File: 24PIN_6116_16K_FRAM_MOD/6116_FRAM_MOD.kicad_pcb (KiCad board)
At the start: 2 copper layers, 17.8 x 35.6 mm, 18 parts, among them J1 Conn_01x02, U1 TL431DBZ, U10 TC5564APL_Adapter, U2 74AHC2G00, U3 STK12C68

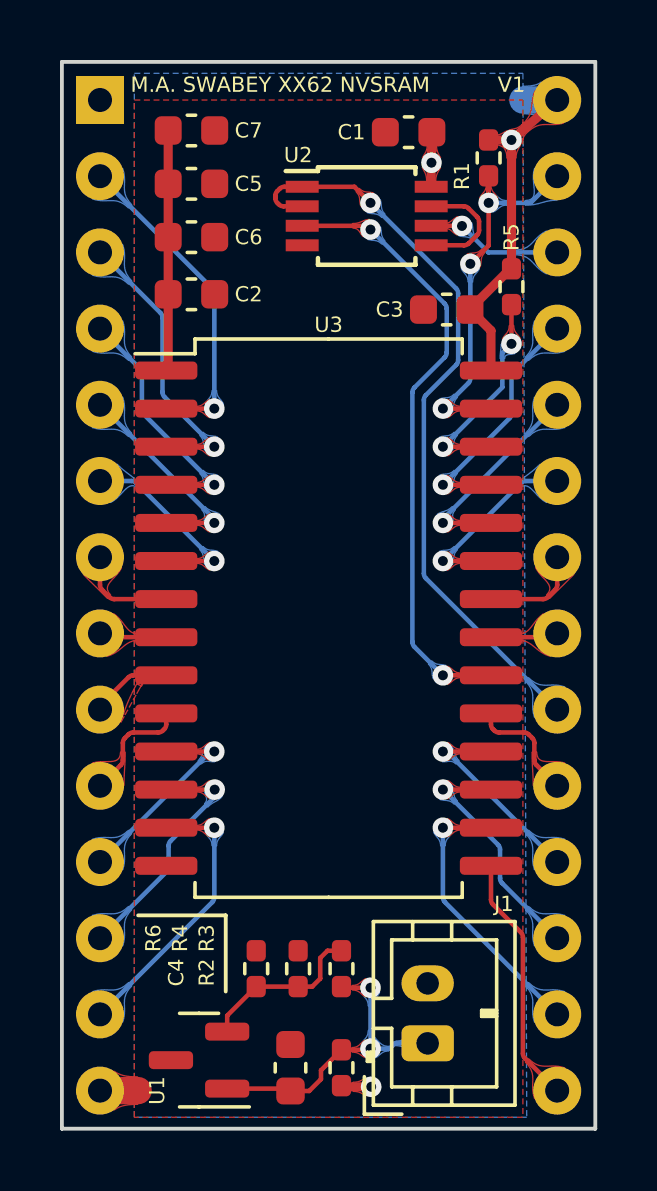
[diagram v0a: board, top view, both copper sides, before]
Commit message: Finished 24PIN 6116 version.
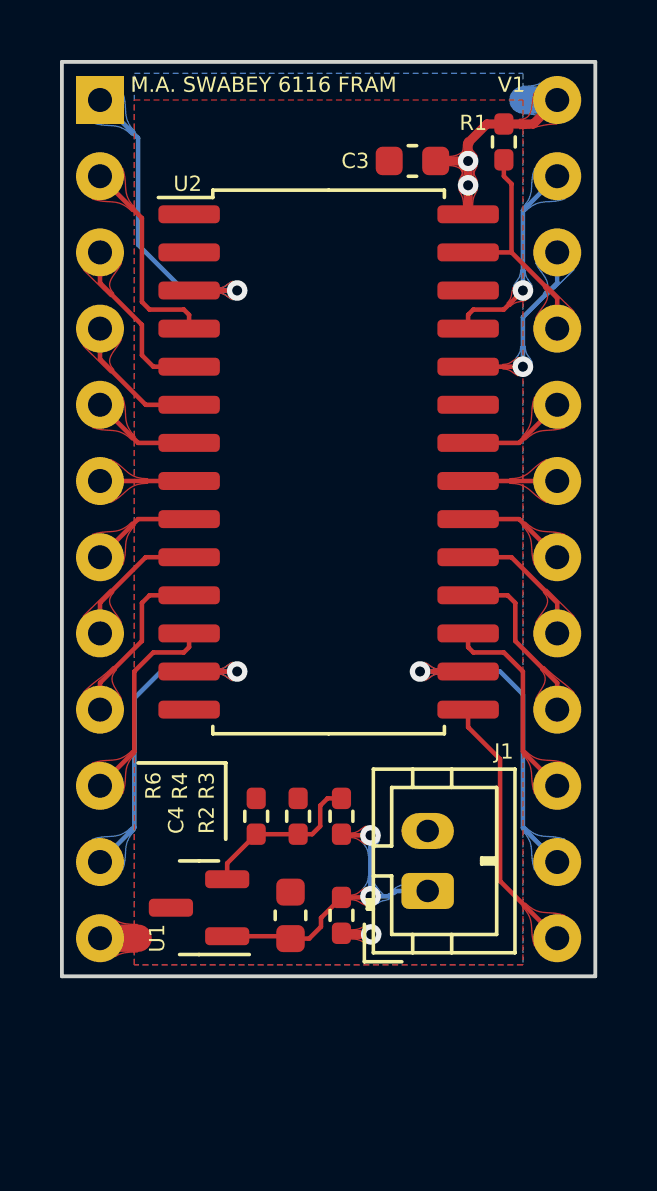
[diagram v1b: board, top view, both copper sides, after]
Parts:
- removed C1: 0.22u, Capacitor_SMD:C_0603_1608Metric
- removed C2, C5, C6, C7: 22u, Capacitor_SMD:C_0603_1608Metric
- removed R5: 10K, Resistor_SMD:R_0402_1005Metric_Pad0.72x0.64mm_HandSolder
- removed U3: STK12C68, Package_SO_Cypress:SOIC-28W_8.7x18.4mm_P1.27mm
- R1: value 10K -> 68K
- U10: footprint Package_DIP_Adapter:DIP-28_W15.24mm_Socket_Adapter -> Package_DIP_Adapter:DIP-24_W15.24mm_Socket_Adapter
- U2: value 74AHC2G00 -> FM16W08-SG; footprint Package_SO:TSSOP-8_3x3mm_P0.65mm -> Package_SO:SOIC-28W_7.5x17.9mm_P1.27mm
- moved U2 8.29 mm to (119.4, 70.5)
- moved C3 5.08 mm to (122.2, 60.5)
- moved U1 5.08 mm to (115.1, 85.3)
- moved C4 5.08 mm to (118.1, 85.6)
- moved J1 5.08 mm to (122.7, 84.8)
- moved R2 5.08 mm to (119.8, 85.6)
- moved R3 5.08 mm to (119.8, 82.3)
- moved R4 5.08 mm to (118.4, 82.3)
- moved R6 5.08 mm to (117.0, 82.3)
- moved R1 0.74 mm to (125.2, 59.8)
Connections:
- U10 pad 1: unconnected-(U10-Pad1) -> /A7
- U10 pad 10: /A0 -> /D1
- U10 pad 11: /D0 -> /D2
- U10 pad 12: /D1 -> GND
- U10 pad 13: /D2 -> /D3
- U10 pad 14: GND -> /D4
- U10 pad 15: /D3 -> /D5
- U10 pad 16: /D4 -> /D6
- U10 pad 17: /D5 -> /D7
- U10 pad 18: /D6 -> /~{CE}
- U10 pad 19: /D7 -> /A10
- U10 pad 2: /A12 -> /A6
- U10 pad 20: /~{CE1} -> /~{OE}
- U10 pad 21: /A10 -> /~{WE}
- U10 pad 22: /~{OE} -> /A9
- U10 pad 23: /A11 -> /A8
- U10 pad 24: /A9 -> VCC
- U10 pad 3: /A7 -> /A5
- U10 pad 4: /A6 -> /A4
- U10 pad 5: /A5 -> /A3
- U10 pad 6: /A4 -> /A2
- U10 pad 7: /A3 -> /A1
- U10 pad 8: /A2 -> /A0
- U10 pad 9: /A1 -> /D0
- U2 pad 1: /~{CE1} -> (no net)
- U2 pad 2: /~{CE1} -> GND
- U2 pad 3: /~{CE_STK} -> /A7
- U2 pad 4: GND -> /A6
- U2 pad 5: Net-(U2-Pad5) -> /A5
- U2 pad 6: /CE2 -> /A4
- U2 pad 7: Net-(U2-Pad5) -> /A3
- U2 pad 8: VCC -> /A2
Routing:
- net /~{CE1}: track 25.0 -> 0.00 mm, vias 1 -> 0
- net /~{CE_STK}: track 20.7 -> 0.00 mm, vias 2 -> 0
- net /A12: track 10.9 -> 0.00 mm, vias 1 -> 0
- net /VCAP: track 8.03 -> 0.00 mm
- net Net-(R5-Pad2): track 7.29 -> 0.00 mm, vias 2 -> 0
- net /A11: track 6.51 -> 0.00 mm, vias 1 -> 0
- net VCC: track 15.3 -> 9.18 mm
- net /~{WE}: track 13.5 -> 7.81 mm, vias 3 -> 0
- net /CE2: track 4.56 -> 0.00 mm, vias 1 -> 0
- net Net-(U2-Pad5): track 3.96 -> 0.00 mm
- net /~{CE}: track 0.00 -> 3.50 mm
- net /D4: track 9.39 -> 11.4 mm
- net /D2: track 9.39 -> 11.3 mm
- net /A4: track 6.51 -> 4.62 mm, vias 1 -> 0
- net /A8: track 8.37 -> 6.91 mm
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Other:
- board size 17.8 x 35.6 mm -> 17.8 x 30.5 mm
- board text added: "M.A. SWABEY 6116 FRAM"
- board text removed: "M.A. SWABEY XX62 NVSRAM"

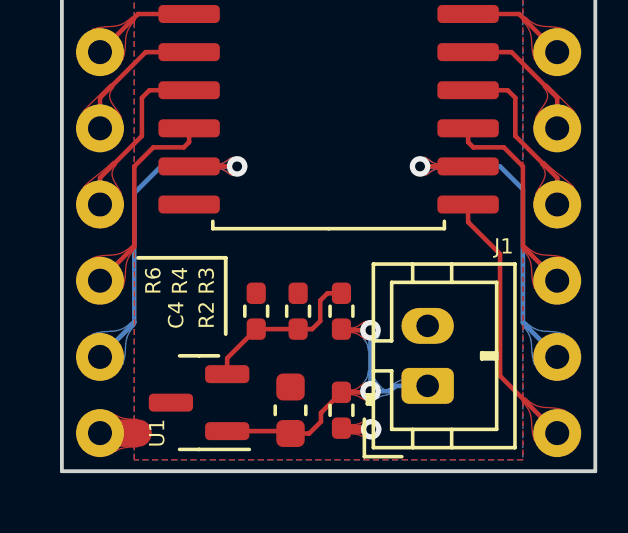
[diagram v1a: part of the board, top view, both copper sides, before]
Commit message: Updated title block on schematics. Minor silkscreen tweak to 24PIN 6116
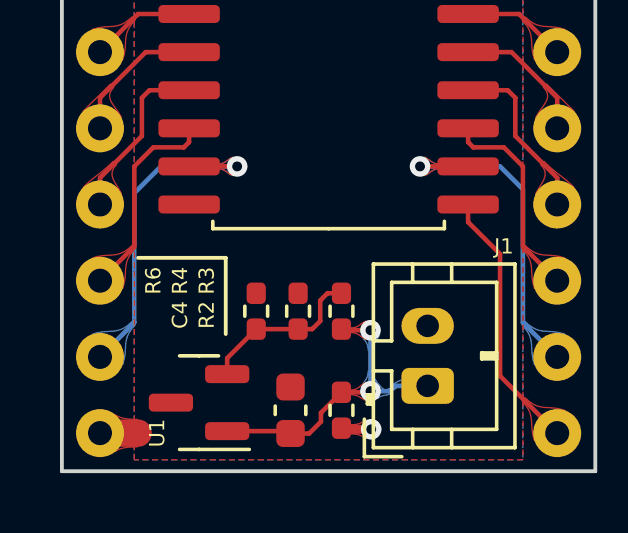
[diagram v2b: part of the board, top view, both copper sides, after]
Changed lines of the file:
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@@
     (property "Sheetname" "")
     (attr smd)
-    (fp_text reference "C4" (at 3.175 -3.81 90) (layer "F.SilkS")
+    (fp_text reference "C4" (at 3.175 -3.683 90) (layer "F.SilkS")
       (effects (font (size 0.508 0.508) (thickness 0.127)))
     )
